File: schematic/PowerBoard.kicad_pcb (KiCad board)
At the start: 2 copper layers, 90.2 x 95.9 mm, 29 parts, among them J1 ToResistor, J2 ToResistor, Q1 IRLB8721PBF, Q2 IRLB8721PBF, U1 PAM2423A

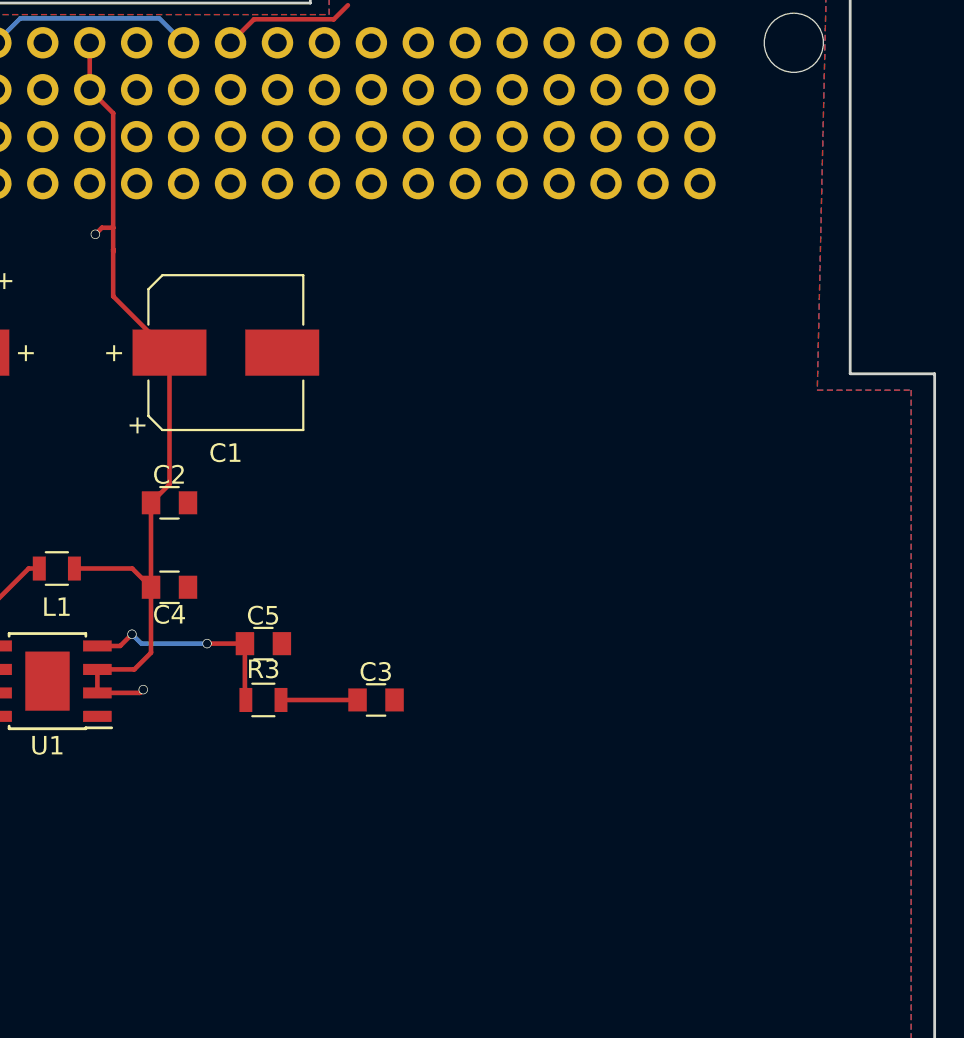
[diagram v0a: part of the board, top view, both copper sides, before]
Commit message: Fixed PC104 conflicts and added i2c debug
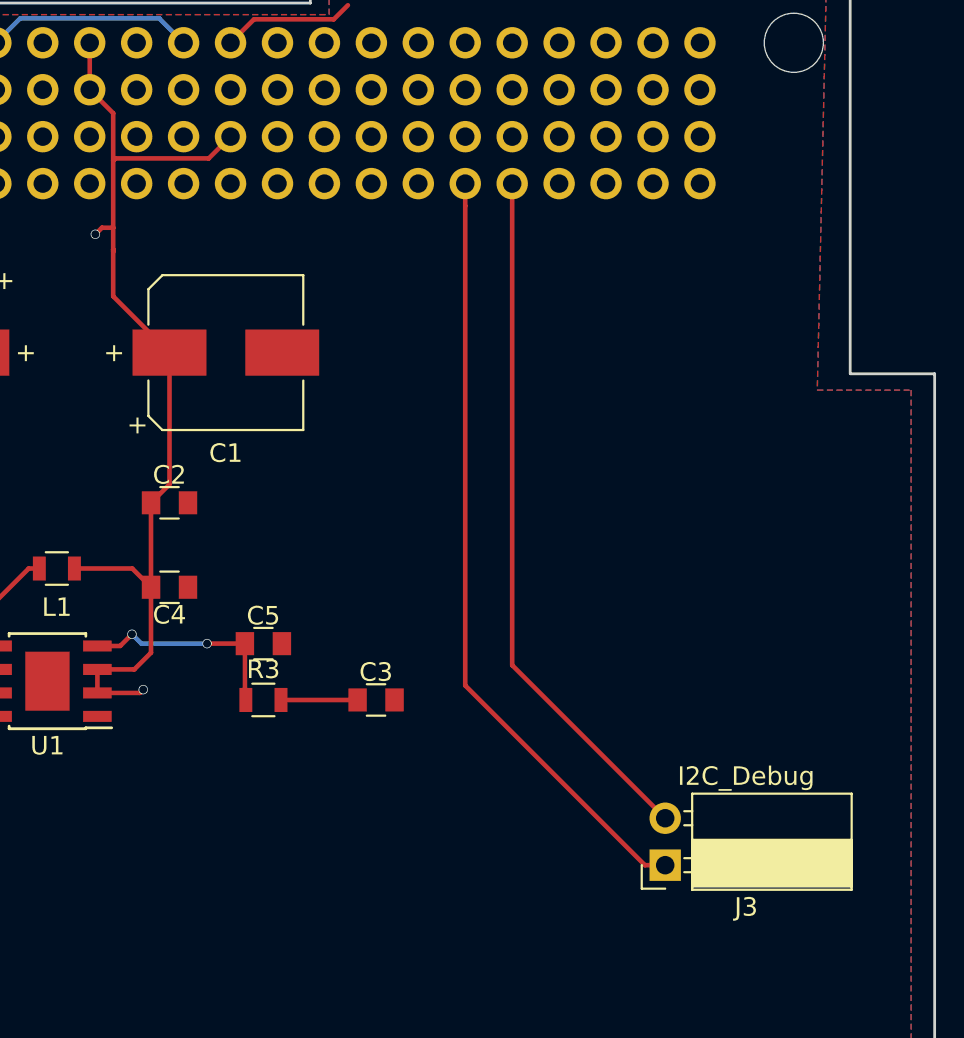
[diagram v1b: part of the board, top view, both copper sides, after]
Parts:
- added J3: I2C_Debug, Socket_Strips:Socket_Strip_Angled_1x02_Pitch2.54mm, F.Cu at (179.7, 97.8)
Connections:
- H1 pad 32: Net-(H1-Pad32) -> +5V
- H1 pad 41: Net-(H1-Pad41) -> I2C_SDA
- H1 pad 43: Net-(H1-Pad43) -> I2C_SCL
- H1 pad 47: Net-(H1-Pad47) -> +5V
- Q1 pad 1: (no net) -> Pri_Deploy
- Q1 pad 3: Pri_Deploy -> GND
- Q1 pad 4: GND -> (no net)
- Q2 pad 1: LineDeploymentDevice -> Pri_Deploy
- Q2 pad 3: Pri_Deploy -> GND
- Q2 pad 4: GND -> (no net)
- Q2 pad 5: LineDeploymentDevice -> (no net)
- Q2 pad 6: LineDeploymentDevice -> (no net)
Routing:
- net I2C_SDA: track 0.00 -> 42.0 mm
- net I2C_SCL: track 0.00 -> 37.8 mm
- net +5V: track 48.1 -> 55.0 mm
- net (no net): track 0.00 -> 2.52 mm
- net GND: track 40.1 -> 37.6 mm

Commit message: Added names
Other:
- board text added: "Matthew Nelson Kenzie Kilcoin William Rickert William Brown Jake Drahos Brian Kempa Ben Sweet Ben Halley Nolan Jessen"
- board text added: "TEAM CYSAT:"
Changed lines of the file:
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@@
   (general
     (thickness 1.6)
-    (drawings 21)
+    (drawings 23)
     (tracks 132)
     (zones 0)
@@
     )
   )
+  (gr_text "Matthew Nelson\nKenzie Kilcoin\nWilliam Rickert\nWilliam Brown\nJake Drahos\nBrian Kempa\nBen Sweet\nBen Halley \nNolan Jessen \n" (at 176.657 85.471) (layer B.SilkS)
+    (effects (font (size 2 2) (thickness 0.3)) (justify left mirror))
+  )
+  (gr_text "TEAM CYSAT:" (at 166.624 67.691) (layer B.SilkS)
+    (effects (font (size 3 3) (thickness 0.3)) (justify mirror))
+  )
   (gr_text + (at 145.1356 70.104) (layer F.SilkS)
     (effects (font (size 1 1) (thickness 0.25)))
@@
   (gr_line (start 189.74 71.25) (end 194.31 71.25) (angle 90) (layer Edge.Cuts) (width 0.15))
   (gr_line (start 189.74 48.26) (end 189.74 71.25) (angle 90) (layer Edge.Cuts) (width 0.15))
+  (segment (start 121.954 131.0885) (end 121.954 132.173) (width 0.25) (layer F.Cu) (net 0))
+  (segment (start 121.954 132.173) (end 121.92 132.207) (width 0.25) (layer F.Cu) (net 0))
+  (segment (start 123.4145 116.674) (end 123.4145 118.0125) (width 0.25) (layer F.Cu) (net 0))
+  (segment (start 123.4145 118.0125) (end 123.3805 118.0465) (width 0.25) (layer F.Cu) (net 0))
   (segment (start 149.86 63.3476) (end 149.2504 63.3476) (width 0.25) (layer F.Cu) (net 1))
   (via (at 148.8948 63.7032) (size 0.508) (drill 0.4318) (layers F.Cu B.Cu) (net 1))
@@
   (segment (start 149.86 63.3476) (end 149.86 64.516) (width 0.25) (layer F.Cu) (net 1))
   (segment (start 149.86 64.516) (end 149.86 64.6684) (width 0.25) (layer F.Cu) (net 1))
-  (segment (start 121.954 131.0885) (end 121.954 132.173) (width 0.25) (layer F.Cu) (net 0))
-  (segment (start 121.954 132.173) (end 121.92 132.207) (width 0.25) (layer F.Cu) (net 0))
-  (segment (start 123.4145 116.674) (end 123.4145 118.0125) (width 0.25) (layer F.Cu) (net 0))
-  (segment (start 123.4145 118.0125) (end 123.3805 118.0465) (width 0.25) (layer F.Cu) (net 0))
   (segment (start 155.031799 59.598201) (end 149.977199 59.598201) (width 0.25) (layer F.Cu) (net 1))
   (segment (start 149.86 57.149995) (end 149.86 59.7154) (width 0.25) (layer F.Cu) (net 1))
